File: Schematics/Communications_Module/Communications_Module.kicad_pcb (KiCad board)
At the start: 4 copper layers, 69.5 x 60 mm, 72 parts, among them J1 USB_B_Micro, J2 SWD_01x04_Pin, J3 Stack Male Edge Connector, Q1 AO3400A, SW1 SW_STM_RESET, SW2 SW_STM_BOOT_MODE, U1 RFM95W-915S2, U2 W25Q128JVS, U3 AMS1117-3.3, U4 LM66100DCKR, U5 LM66100DCKR, U6 LM66100DCKR, U7 STM32F103CBT6, U8 ACS70331EOLC, U9 ISO1042BDWVR, Y1 X322516MMB4SI

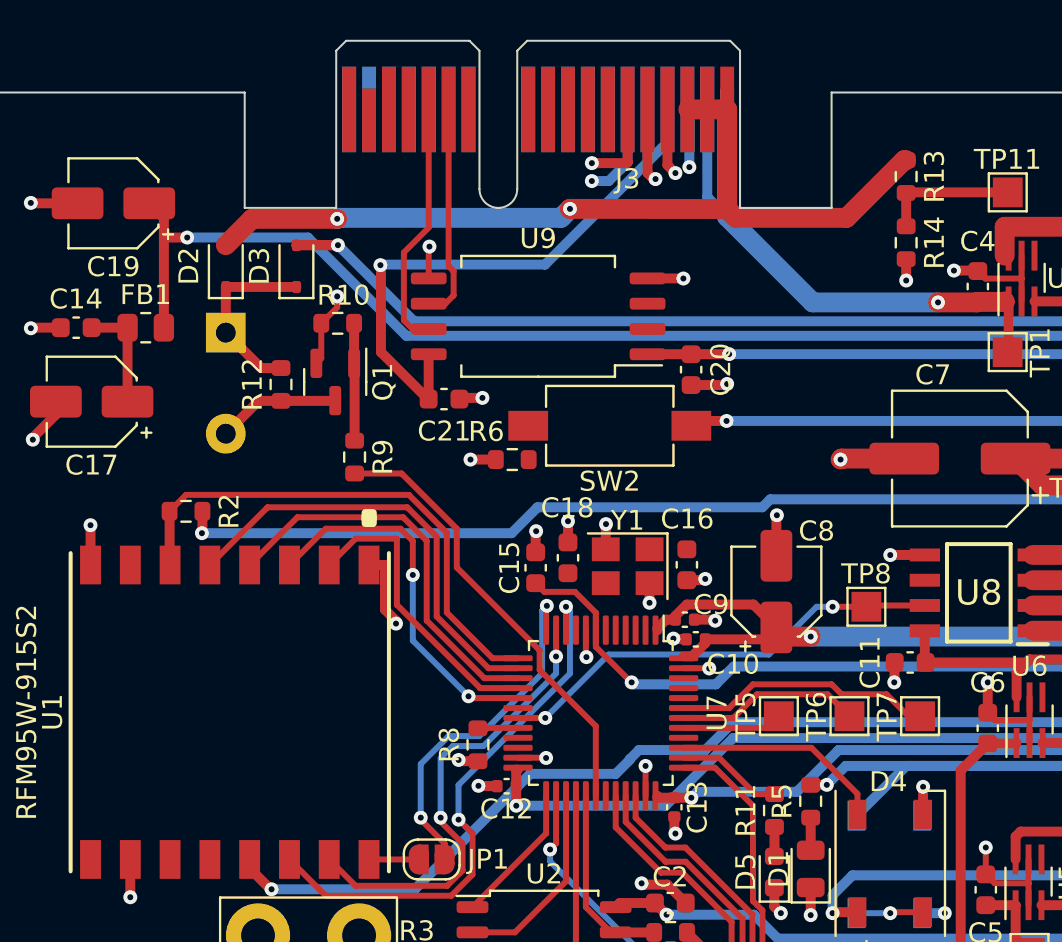
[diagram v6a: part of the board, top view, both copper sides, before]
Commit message: Layout done except antenna trace
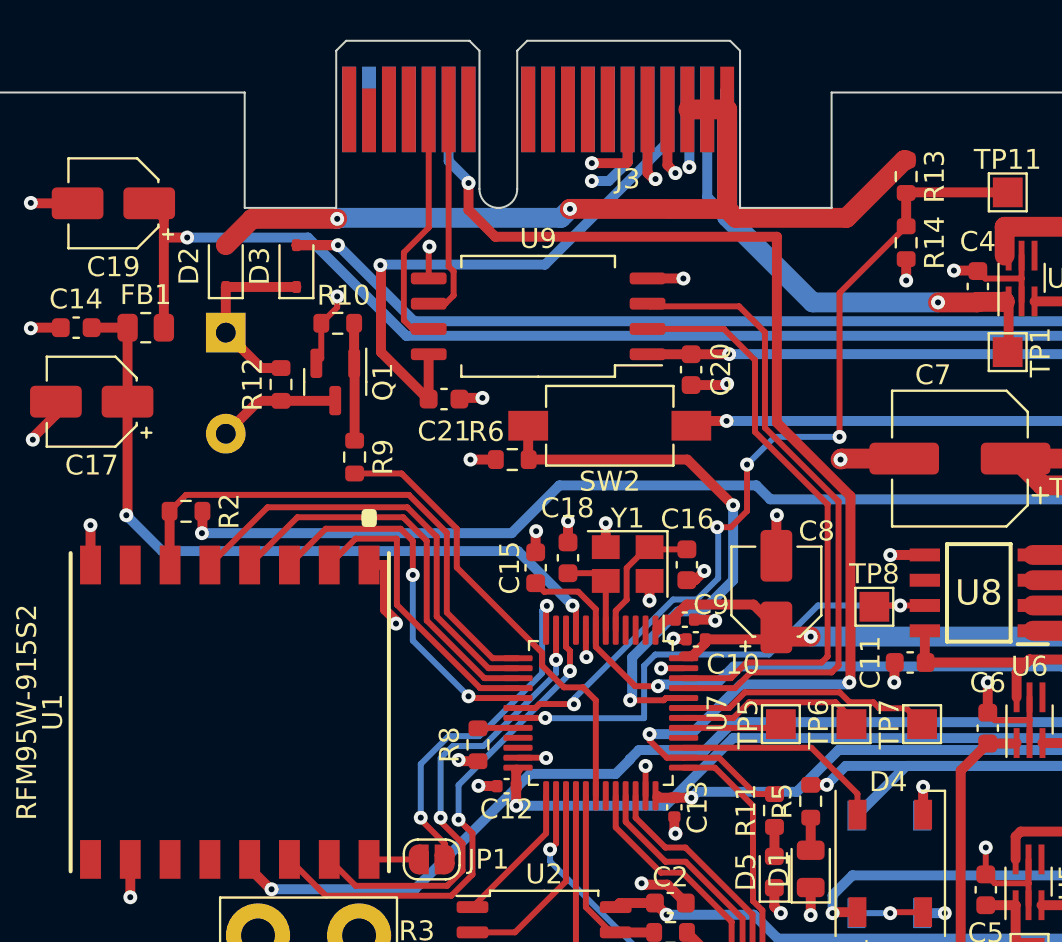
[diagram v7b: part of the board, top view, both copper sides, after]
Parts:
- moved TP7 0.41 mm to (158.3, 109.1)
- moved TP5 0.41 mm to (151.2, 109.1)
- moved TP6 0.41 mm to (154.8, 109.1)
- moved TP8 0.40 mm to (155.9, 103.2)
- moved Y1 0.11 mm to (143.5, 101.0)
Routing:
- net DB_LED: track 5.32 -> 64.6 mm, vias 0 -> 3
- net BATT_SENSE: track 6.79 -> 43.7 mm, vias 0 -> 4
- net CAN_RX: track 0.00 -> 33.0 mm
- net +3.3VA: track 5.53 -> 37.1 mm, vias 0 -> 2
- net CAN_TX: track 0.00 -> 30.1 mm
- net BOOT0: track 0.00 -> 28.3 mm, vias 0 -> 2
- net OSC_IN: track 0.00 -> 6.86 mm
- net OSC_OUT: track 0.00 -> 4.54 mm
- net CURR_SENSE: track 22.8 -> 25.9 mm
- net DIO0_RF: track 27.7 -> 25.4 mm
- net +3.3V: track 525.5 -> 526.1 mm
- net BUZZER: track 22.6 -> 23.2 mm
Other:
- board text added: "Gross Trace Tracker (they all are, but here's the worst): - STM Reset - USB Diff Pair? - SCK_FL - Curr_sense - MOSI_RF - RF DIOx traces - Buzzer (PWM right? something should prob be done about that one) - Can_Rx/Tx traces? - batt_sense"
- board text added: "make sure osc circuit is good"
- board text added: "worried about noise (especially from buzzer) on analogue trace"
- board text removed: "Going to be awful: - DB_LED - Batt_sense - 3.3VA - oscillator"
- board text removed: "Gross Trace Tracker (they all are, but here's the worst): - STM Reset - USB Diff Pair? - SCK_FL - Curr_sense - MOSI_RF - RF DIOx traces - Buzzer (PWM right? something should prob be done about that one)"

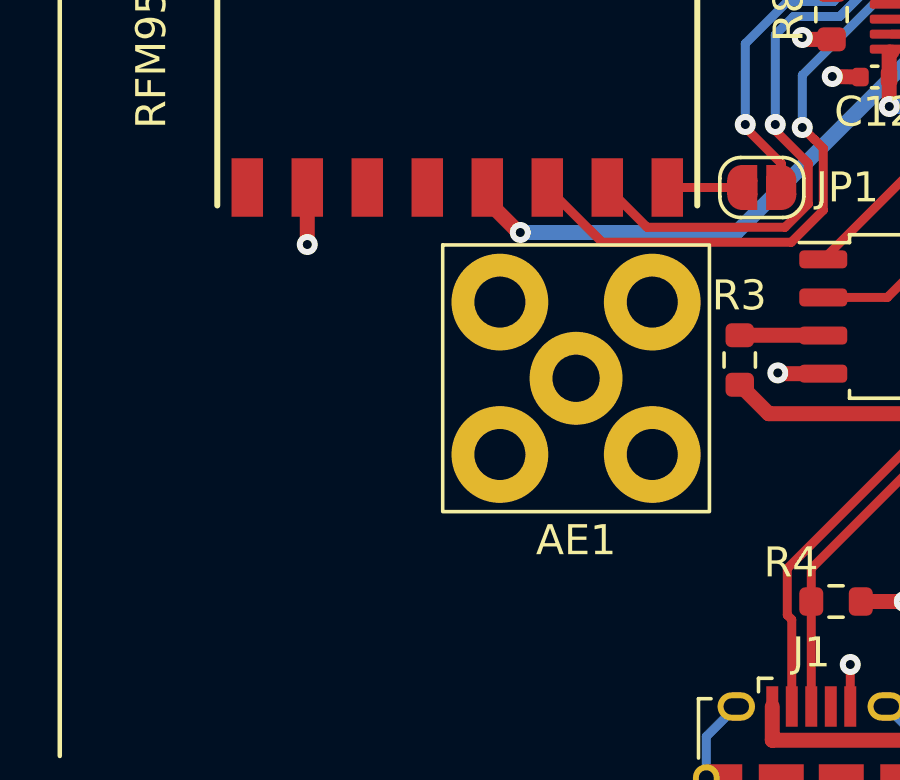
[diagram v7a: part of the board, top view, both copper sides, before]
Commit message: antenna trace? Via fencing
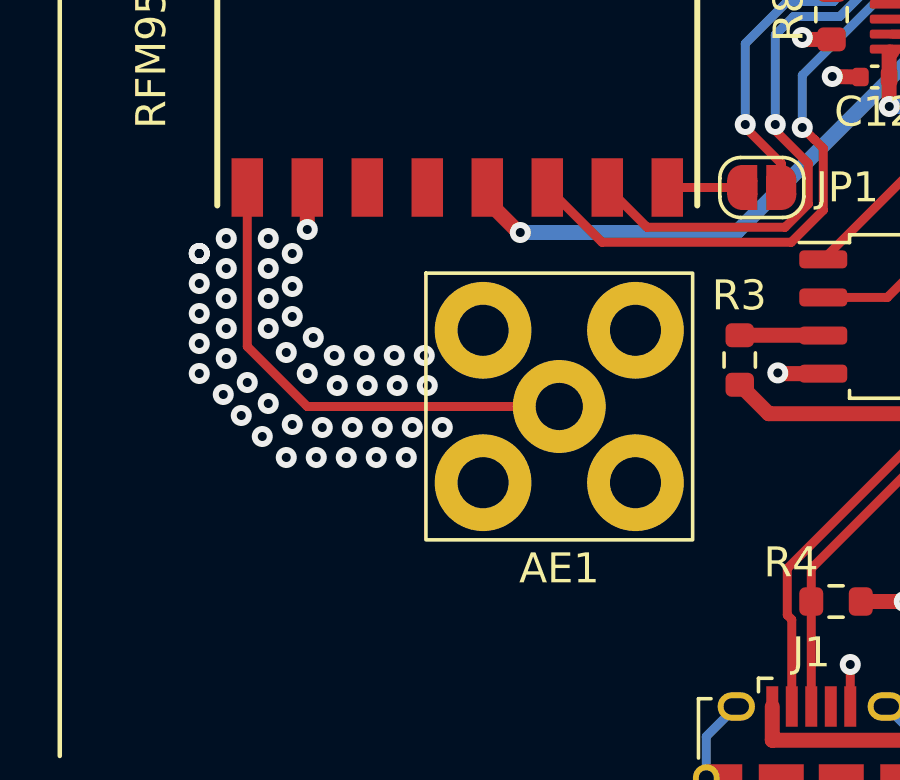
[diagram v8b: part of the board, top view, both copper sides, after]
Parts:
- moved AE1 1.09 mm to (126.9, 123.2)
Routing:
- net Net-(AE1-A): track 0.00 -> 16.5 mm
- net GND: track 109.2 -> 108.7 mm, vias 51 -> 96
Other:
- board text added: "need to confirm this trace via fence can block up to like 20 GHz"
